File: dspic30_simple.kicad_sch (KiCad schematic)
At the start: 21 parts, among them J1 Jack-DC, J2 Conn_01x19_Pin, J4 Conn_01x21_Pin, SW1 SW_Push, U1 PIC18F4550-IP, U2 L7805, Y1 Crystal

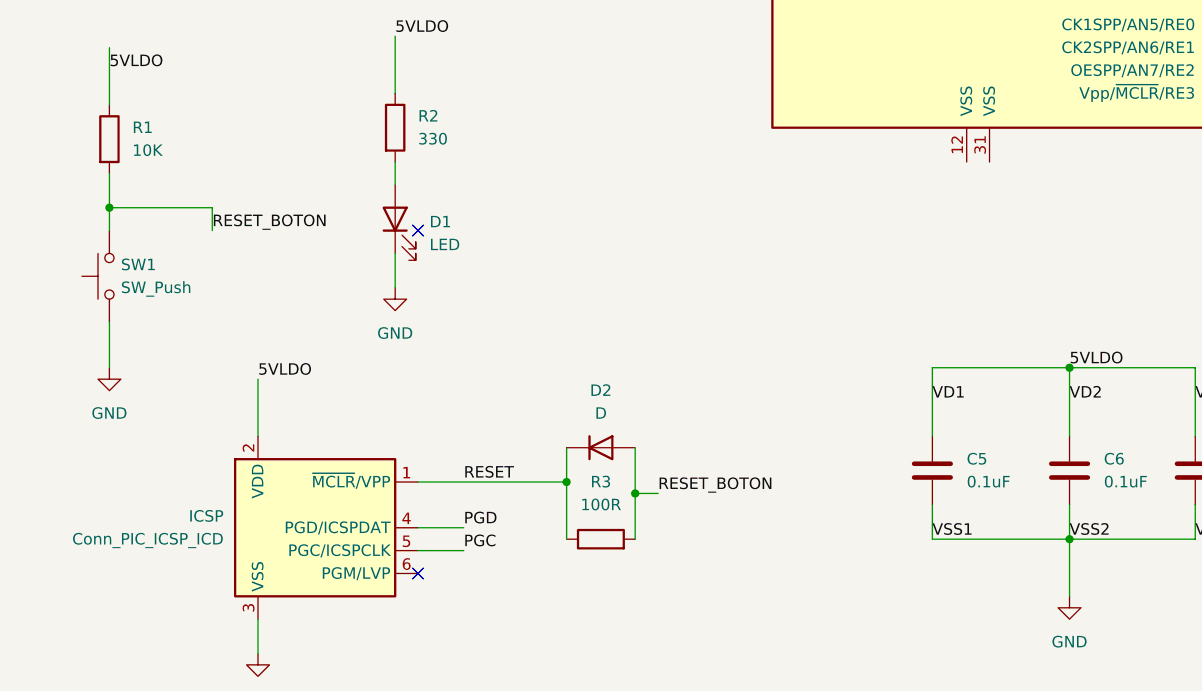
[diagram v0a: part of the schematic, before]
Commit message: fix GDN not connnected
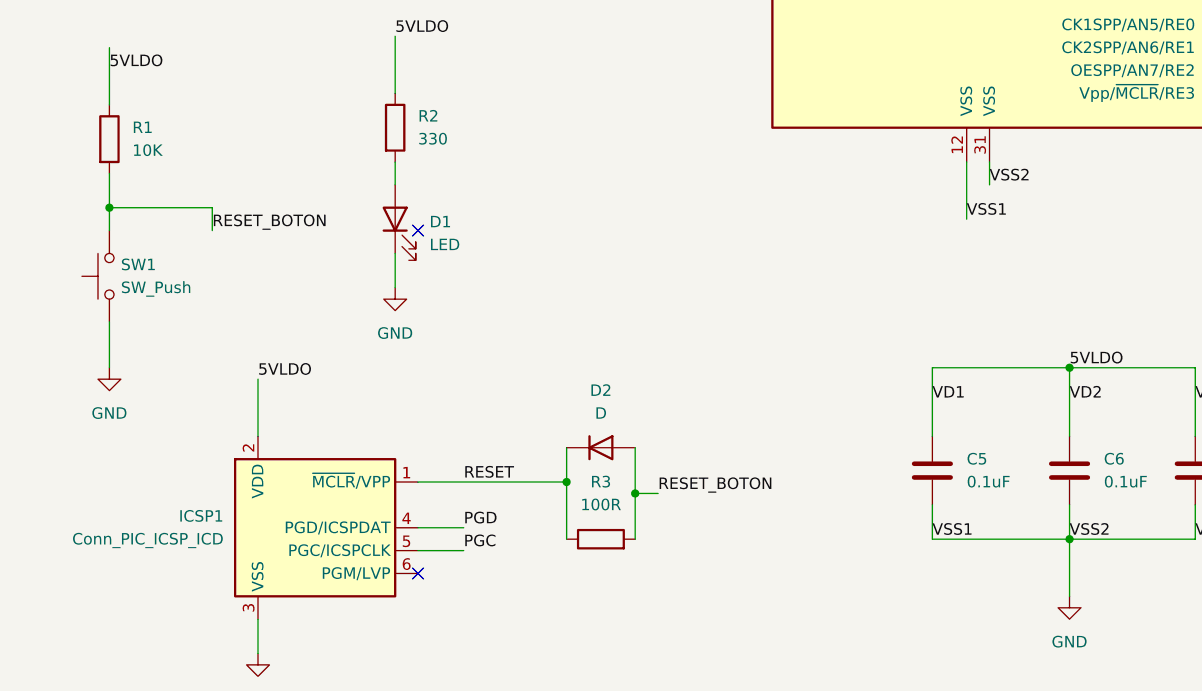
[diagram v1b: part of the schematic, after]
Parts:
- renumbered ICSP to ICSP1
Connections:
- net GND: now also U1.12 (VSS), U1.31 (VSS)
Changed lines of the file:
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@@
 	(wire
 		(pts
+			(xy 171.45 109.22) (xy 171.45 106.68)
+		)
+		(stroke
+			(width 0)
+			(type default)
+		)
+	)
+	(wire
+		(pts
 			(xy 113.03 147.32) (xy 107.95 147.32)
 		)
@@
 	(wire
 		(pts
+			(xy 168.91 106.68) (xy 168.91 113.03)
+		)
+		(stroke
+			(width 0)
+			(type default)
+		)
+	)
+	(wire
+		(pts
 			(xy 234.95 134.62) (xy 241.3 134.62)
 		)
@@
 		)
 	)
+	(label "VSS1"
+		(at 168.91 113.03 0)
+		(fields_autoplaced yes)
+		(effects
+			(font
+				(size 1.27 1.27)
+			)
+			(justify left bottom)
+		)
+	)
 	(label "PGD"
 		(at 208.28 55.88 0)
@@
 		)
 	)
+	(label "VSS2"
+		(at 171.45 109.22 0)
+		(fields_autoplaced yes)
+		(effects
+			(font
+				(size 1.27 1.27)
+			)
+			(justify left bottom)
+		)
+	)
 	(label "RE2"
 		(at 245.11 63.5 0)
@@
 		(dnp no)
 		(fields_autoplaced yes)
-		(property "Reference" "ICSP"
+		(property "Reference" "ICSP1"
 			(at 86.36 146.0499 0)
 			(effects
@@
 			(project ""
 				(path "/c57c8b8a-cb5c-45d3-8c1c-ff7cf62f6723"
-					(reference "ICSP")
+					(reference "ICSP1")
 					(unit 1)
 				)
